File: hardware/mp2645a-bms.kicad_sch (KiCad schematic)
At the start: 0 parts

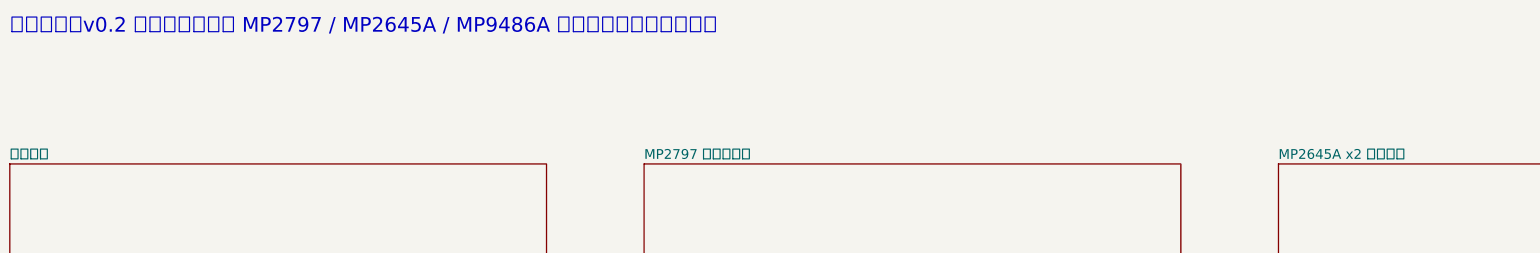
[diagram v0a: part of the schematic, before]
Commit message: v0.3：主动均衡改为 MP2643 ×7（MPS 客供），光耦跨电位控制，逐对均衡策略，BOM 与成本估算
- docs/03：均衡章节按 MP2643 手册 Rev1.1 重写（外围逐件点名、电流/限压计算、光耦接口、线束与发热）
- firmware：7 对 EN/MODE 输出，边界电荷盈亏定方向，相邻不同时开，收敛仿真测试
- tools/bms_calc.py：MP2643 手册公式；tools/jlc_api.py：嘉立创料号接口；tools/cost.py：成本估算
- docs/02-BOM.csv v0.3（81 行，带立创编号与来源），docs/05-成本估算.md
- KiCad 骨架更新（03 子图接口、网络类）

Co-Authored-By: Claude Opus 5.5 <noreply@anthropic.com>
Claude-Session: https://claude.ai/code/session_01EyFjq1nqLUmfVYESj2uYXd
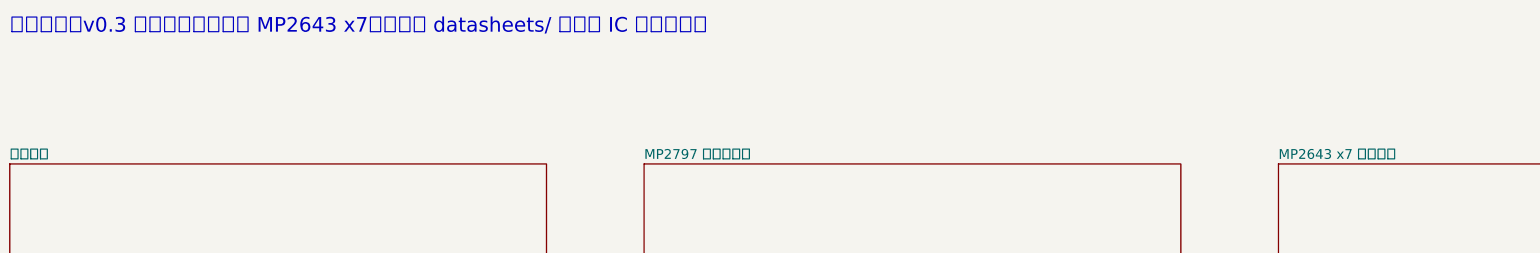
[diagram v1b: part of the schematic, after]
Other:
- sheet MP2645A x2 主动均衡 renamed MP2643 x7 主动均衡
- note added: "层次结构（v0.3 骨架）：主动均衡 MP2643 x7；电路按 datasheets/ 手册逐 IC 核对后再画"
- note removed: "层次结构（v0.2 骨架）：电路待 MP2797 / MP2645A / MP9486A 正式数据手册核对后再画"
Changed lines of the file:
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@@
 		(title "8S LFP 200A BMS — 总图")
 		(date "2026-09-26")
-		(rev "v0.2-skeleton")
+		(rev "v0.3-skeleton")
 		(company "MP2645A-BMS")
-		(comment 1 "8S LiFePO4 200A BMS · MPS MP2797 + MP2645A")
+		(comment 1 "8S LiFePO4 200A BMS · MPS MP2797 + MP2643x7")
 	)
-	(text "层次结构（v0.2 骨架）：电路待 MP2797 / MP2645A / MP9486A 正式数据手册核对后再画"
+	(text "层次结构（v0.3 骨架）：主动均衡 MP2643 x7；电路按 datasheets/ 手册逐 IC 核对后再画"
 		(exclude_from_sim no)
 		(at 20 20 0)
@@
 			(color 0 0 0 0.0000)
 		)
-		(property "Sheetname" "MP2645A x2 主动均衡"
+		(property "Sheetname" "MP2643 x7 主动均衡"
 			(at 280 49.2 0)
 			(effects

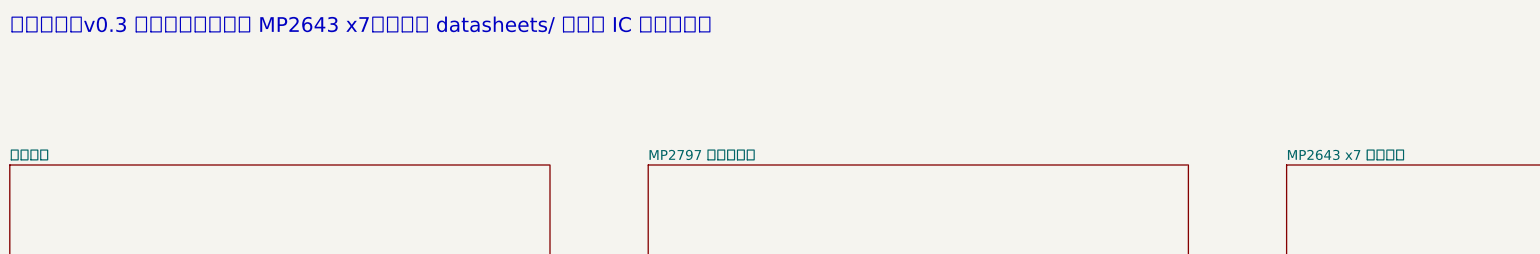
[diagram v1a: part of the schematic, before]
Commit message: 主动均衡改为分立开关电容（方案 B）：均衡部分约 ¥186→¥35/块
- 8 个互补半桥 AO3400A/AO3401A（基础库）+ 74LVC1G17 本节供电驱动，7 级飞电容 3×100µF，MCU BAL_CLK 50kHz 逐级电容耦合
- 固件：单一时钟使能；顶部/静置才开；压差>300mV 或任一节<3.0V 禁止；测试 37/37
- 计算器：sc_equalizer 模型（100mV≈0.21A，300mV≈0.62A）；测试 21/21
- BOM/成本：整板元器件 10 块 ¥359→¥202/块，100 块 ¥267→¥156/块
- 均衡端子改国产 2×5 Micro-Fit 兼容 C3030WV-2x5P（实测 3.0mm），节点保险丝 3A 1206

Co-Authored-By: Claude Opus 5.5 <noreply@anthropic.com>
Claude-Session: https://claude.ai/code/session_01EyFjq1nqLUmfVYESj2uYXd
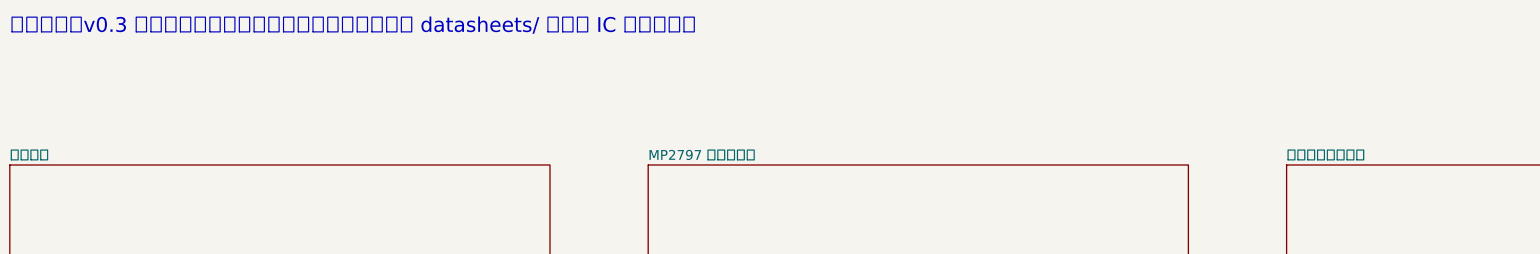
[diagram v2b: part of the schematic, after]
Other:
- sheet MP2643 x7 主动均衡 renamed 开关电容主动均衡
- note added: "层次结构（v0.3 骨架）：主动均衡为分立开关电容；电路按 datasheets/ 手册逐 IC 核对后再画"
- note removed: "层次结构（v0.3 骨架）：主动均衡 MP2643 x7；电路按 datasheets/ 手册逐 IC 核对后再画"
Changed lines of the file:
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@@
 		(rev "v0.3-skeleton")
 		(company "MP2645A-BMS")
-		(comment 1 "8S LiFePO4 200A BMS · MPS MP2797 + MP2643x7")
+		(comment 1 "8S LiFePO4 200A BMS · MPS MP2797 + 开关电容均衡")
 	)
-	(text "层次结构（v0.3 骨架）：主动均衡 MP2643 x7；电路按 datasheets/ 手册逐 IC 核对后再画"
+	(text "层次结构（v0.3 骨架）：主动均衡为分立开关电容；电路按 datasheets/ 手册逐 IC 核对后再画"
 		(exclude_from_sim no)
 		(at 20 20 0)
@@
 			(color 0 0 0 0.0000)
 		)
-		(property "Sheetname" "MP2643 x7 主动均衡"
+		(property "Sheetname" "开关电容主动均衡"
 			(at 280 49.2 0)
 			(effects
